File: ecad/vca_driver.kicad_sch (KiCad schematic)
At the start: 5 parts, among them Q2 Q_PNP, Q3 Q_NPN, U1 MCP6001R

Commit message: stuff
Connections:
- net DRV_CURR_Vref: no longer U1.3 (+)
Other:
- note added: "level-shifter stage"
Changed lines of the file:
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@@
+		)
+	)
+	(text "level-shifter stage"
+		(exclude_from_sim no)
+		(at 74.676 91.44 0)
+		(effects
+			(font
+				(size 1.27 1.27)
+			)
 		)
 	)
@@
 	(hierarchical_label "DRV_CURR_Vref"
 		(shape input)
-		(at 95.25 91.44 180)
+		(at 63.5 91.44 180)
 		(effects
 			(font
@@
 		)
 	)
-	(group ""
-		(members "7da5fe76-c194-4e79-b321-c29380be2a89" "7fe1ba20-d693-422a-b992-88df42c37689"
-			"9cf646c3-572a-464c-8c83-e4a098683738"
-		)
-	)

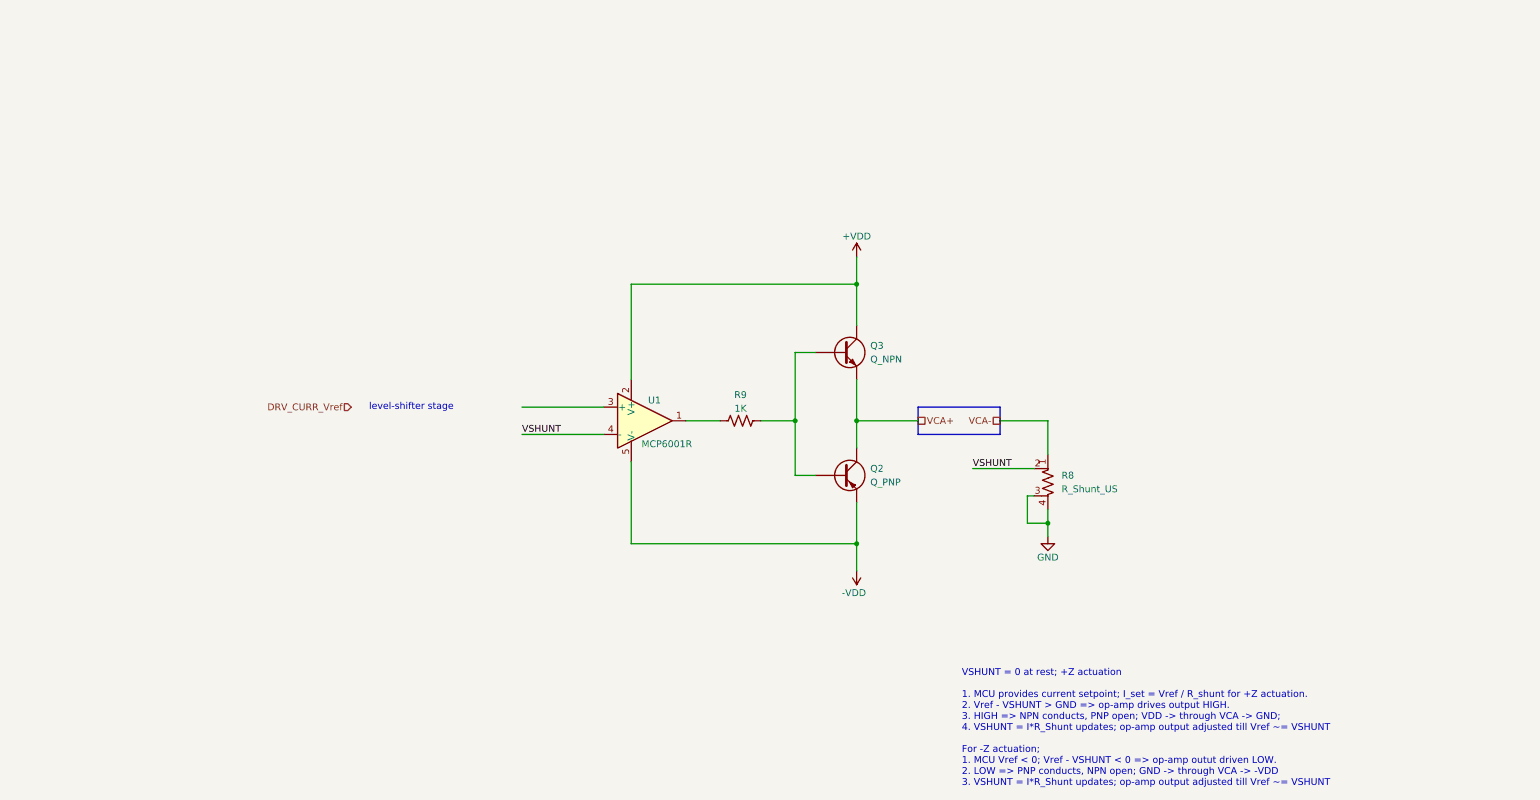
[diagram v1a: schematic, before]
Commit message: vca op-amp, transistor selection; heat calcs
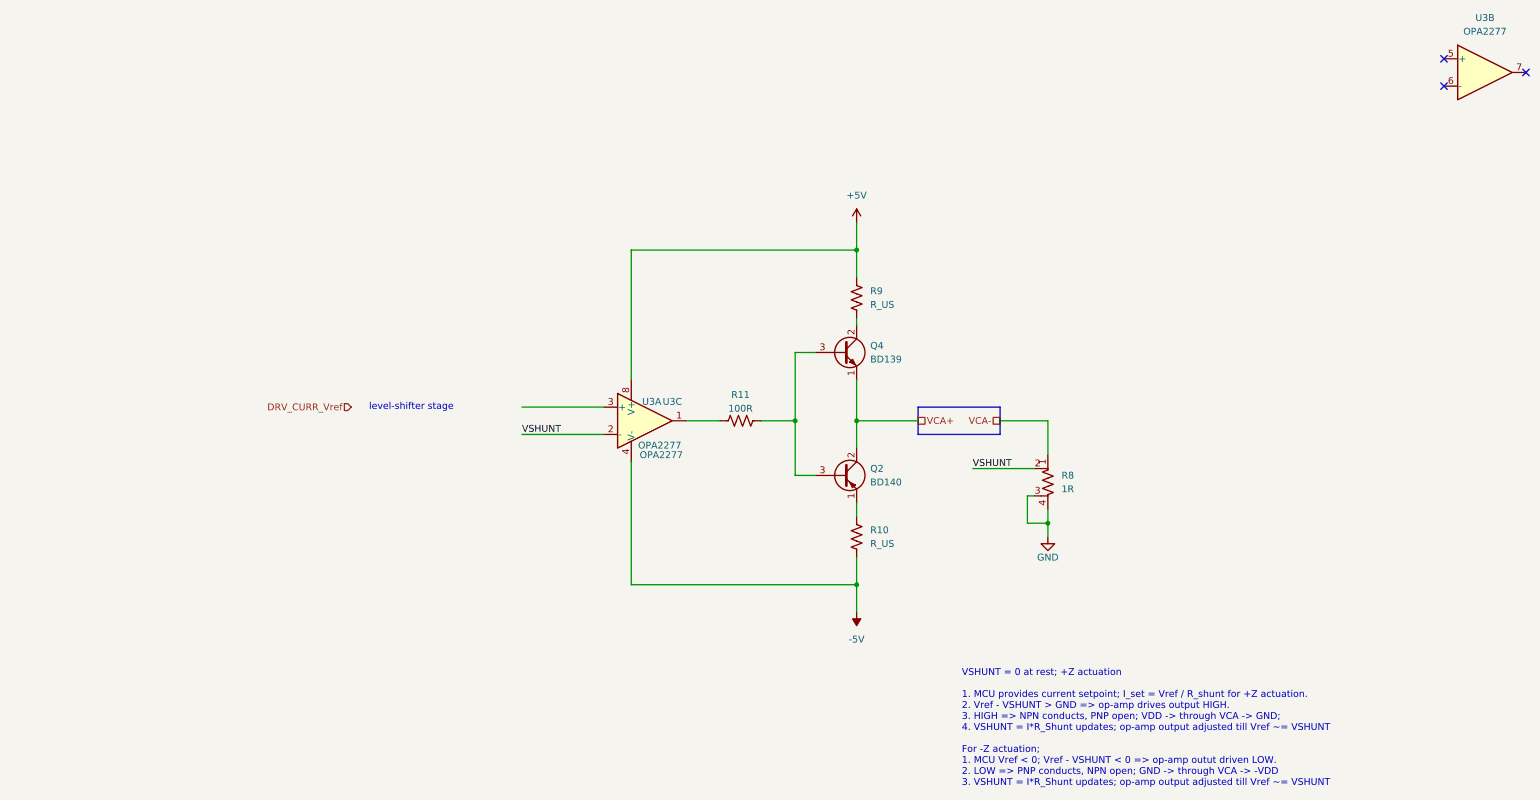
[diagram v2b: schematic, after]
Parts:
- removed Q2: Q_PNP, symbol Device:Q_PNP
- removed Q3: Q_NPN, symbol Device:Q_NPN
- removed U1: MCP6001R, Package_TO_SOT_SMD:SOT-23-5, symbol Amplifier_Operational:MCP6001R
- added Q2: BD140, Package_TO_SOT_THT:TO-126-3_Vertical, symbol Transistor_BJT:BD140
- added Q4: BD139, Package_TO_SOT_THT:TO-126-3_Vertical, symbol Transistor_BJT:BD139
- added R10: R_US, symbol Device:R_US
- added R11: 100R, symbol Device:R_US
- added U3: OPA2277, symbol Amplifier_Operational:OPA2277
- R8: value R_Shunt_US -> 1R
- R9: value 1K -> R_US
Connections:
- net VCA+: now also Q2.2 (C), Q4.1 (E)
- net VSHUNT: now also U3.2 (-)
- net at R9.2: now also Q4.2 (C)
- net +5V: now reaches R9.1
- net +5V: now also U3.8 (V+)
- new net: R11.2, U3.1
- new net: Q2.1 (E), R10.1
- new net: Q2.3 (B), Q4.3 (B), R11.1
- new net -5V: R10.2, U3.4 (V-)
- no-connect marks 0 -> 3

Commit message: more sizing
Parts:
- added C5, C9: 10uF, symbol Device:C_Small
- added R12: 100R, symbol Device:R_US
- R10, R9: value R_US -> 2-10R
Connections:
- net +5V: now also C5.1
- net -5V: now also C9.1
- net GND: now also C5.2, C9.2
- net at R11.2, U3.1: now also R12.2
- net at Q4.3 (B), R11.1: no longer Q2.3 (B)
- new net: Q2.3 (B), R12.1
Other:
- moved on the sheet: Q4, R11, R9

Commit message: pp
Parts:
- added C10, C11: 0.1uF, symbol Device:C_Small
- added C12: 10nF, symbol Device:C_Small
- added D2: BAT54W, Package_TO_SOT_SMD:SOT-323_SC-70, symbol Diode:BAT54W
- added R13: 1K, symbol Device:R_US
- added R14: 47K, symbol Device:R_US
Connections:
- net +5V: now also C10.1
- net -5V: now also C11.1
- net GND: now also C10.2, C11.2, R14.2
- net VCA+: now also Q2.1 (E); no longer Q2.2 (C)
- net VSHUNT: now also R13.1; no longer U3.2 (-)
- net at R11.2, R12.2, U3.1: now also C12.2
- net at U3.3 (+): now also R14.1
- net at R10.1: now also Q2.2 (C); no longer Q2.1 (E)
- new net: C12.1, R13.2, U3.2 (-)
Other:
- moved on the sheet: C5, C9, U3A, U3C

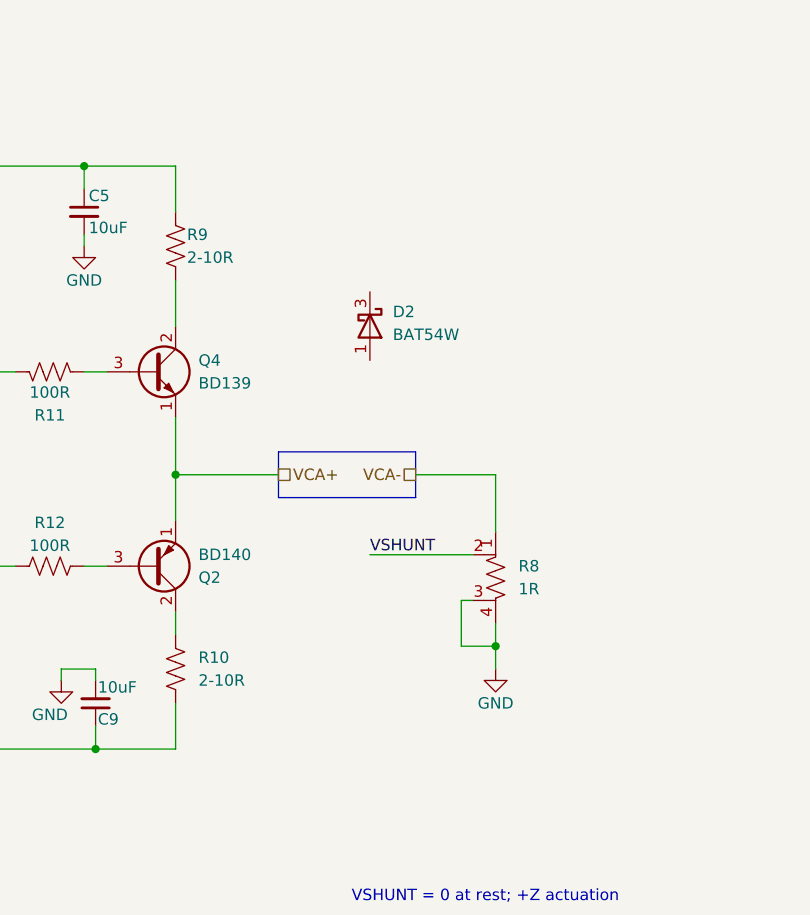
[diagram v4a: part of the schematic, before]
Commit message: diodes for L di/dt
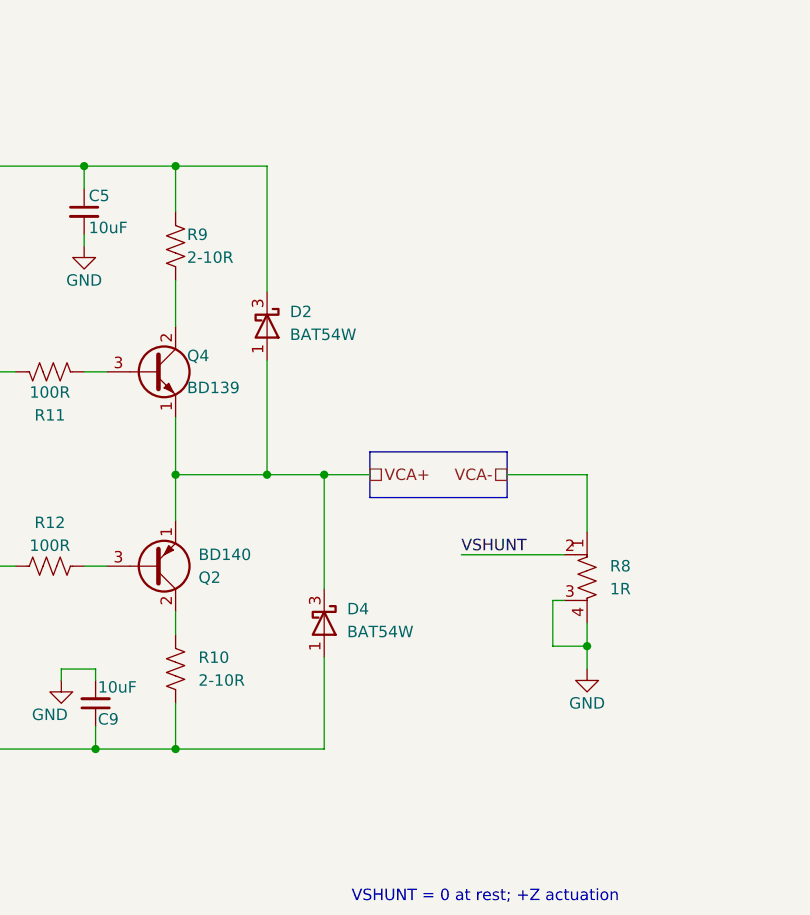
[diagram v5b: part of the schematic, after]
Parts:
- added D4: BAT54W, Package_TO_SOT_SMD:SOT-323_SC-70, symbol Diode:BAT54W
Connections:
- net +5V: now also D2.3 (K)
- net -5V: now also D4.1 (A)
- net VCA+: now also D2.1 (A), D4.3 (K)
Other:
- moved on the sheet: D2, R8

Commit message: vca sims
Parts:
- added R19: 500K, symbol Device:R_US
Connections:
- net at C12.1, R13.2, U3.2 (-): now also R19.1
- net at C12.2, R11.2, R12.2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: now also R19.2
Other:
- note added: "Some sort of clamp to limit max Vref to ~0.3V"
- moved on the sheet: C12
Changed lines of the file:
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@@
+		)
+	)
+	(text "Some sort of clamp to limit max Vref to ~0.3V"
+		(exclude_from_sim no)
+		(at 77.978 82.042 0)
+		(effects
+			(font
+				(size 1.27 1.27)
+			)
 		)
 	)
@@
 	)
 	(junction
+		(at 100.33 104.14)
+		(diameter 0)
+		(color 0 0 0 0)
+	)
+	(junction
 		(at 100.33 96.52)
 		(diameter 0)
@@
 	(junction
 		(at 148.59 124.46)
+		(diameter 0)
+		(color 0 0 0 0)
+	)
+	(junction
+		(at 123.19 104.14)
 		(diameter 0)
 		(color 0 0 0 0)
@@
 	(wire
 		(pts
+			(xy 100.33 104.14) (xy 100.33 96.52)
+		)
+		(stroke
+			(width 0)
+			(type default)
+		)
+	)
+	(wire
+		(pts
 			(xy 97.79 96.52) (xy 100.33 96.52)
 		)
@@
 	(wire
 		(pts
+			(xy 111.76 109.22) (xy 100.33 109.22)
+		)
+		(stroke
+			(width 0)
+			(type default)
+		)
+	)
+	(wire
+		(pts
 			(xy 157.48 119.38) (xy 157.48 124.46)
 		)
@@
 	(wire
 		(pts
-			(xy 118.11 105.41) (xy 123.19 105.41)
+			(xy 118.11 104.14) (xy 123.19 104.14)
 		)
 		(stroke
@@
 	(wire
 		(pts
+			(xy 123.19 104.14) (xy 123.19 109.22)
+		)
+		(stroke
+			(width 0)
+			(type default)
+		)
+	)
+	(wire
+		(pts
 			(xy 135.89 82.55) (xy 139.7 82.55)
 		)
@@
 	(wire
 		(pts
+			(xy 119.38 109.22) (xy 123.19 109.22)
+		)
+		(stroke
+			(width 0)
+			(type default)
+		)
+	)
+	(wire
+		(pts
 			(xy 157.48 72.39) (xy 157.48 77.47)
 		)
@@
 	(wire
 		(pts
-			(xy 113.03 105.41) (xy 100.33 105.41)
+			(xy 113.03 104.14) (xy 100.33 104.14)
 		)
 		(stroke
@@
 	(wire
 		(pts
+			(xy 123.19 104.14) (xy 123.19 93.98)
+		)
+		(stroke
+			(width 0)
+			(type default)
+		)
+	)
+	(wire
+		(pts
 			(xy 147.32 67.31) (xy 147.32 68.58)
 		)
@@
 	(wire
 		(pts
-			(xy 100.33 105.41) (xy 100.33 96.52)
-		)
-		(stroke
-			(width 0)
-			(type default)
-		)
-	)
-	(wire
-		(pts
 			(xy 203.2 113.03) (xy 203.2 115.57)
 		)
@@
 	(wire
 		(pts
+			(xy 100.33 104.14) (xy 100.33 109.22)
+		)
+		(stroke
+			(width 0)
+			(type default)
+		)
+	)
+	(wire
+		(pts
 			(xy 71.12 91.44) (xy 104.14 91.44)
 		)
@@
 		(pts
 			(xy 135.89 93.98) (xy 135.89 82.55)
-		)
-		(stroke
-			(width 0)
-			(type default)
-		)
-	)
-	(wire
-		(pts
-			(xy 123.19 105.41) (xy 123.19 93.98)
 		)
 		(stroke
@@
 	(symbol
 		(lib_id "Device:C_Small")
-		(at 115.57 105.41 90)
+		(at 115.57 104.14 90)
 		(unit 1)
 		(body_style 1)
@@
 		(dnp no)
 		(property "Reference" "C12"
-			(at 114.808 104.14 90)
+			(at 114.808 102.87 90)
 			(show_name no)
 			(do_not_autoplace no)
@@
 		)
 		(property "Value" "10nF"
-			(at 121.412 104.14 90)
+			(at 121.412 102.87 90)
 			(show_name no)
 			(do_not_autoplace no)
@@
 		)
 		(property "Footprint" ""
-			(at 115.57 105.41 0)
+			(at 115.57 104.14 0)
 			(hide yes)
 			(show_name no)
@@
 		)
 		(property "Datasheet" ""
-			(at 115.57 105.41 0)
+			(at 115.57 104.14 0)
 			(hide yes)
 			(show_name no)
@@
 		)
 		(property "Description" "Unpolarized capacitor, small symbol"
-			(at 115.57 105.41 0)
+			(at 115.57 104.14 0)
 			(hide yes)
 			(show_name no)
@@
 					(unit 1)
 				)
+			)
+		)
+	)
+	(symbol
+		(lib_id "Device:R_US")
+		(at 115.57 109.22 90)
+		(mirror x)
+		(unit 1)
+		(body_style 1)
+		(exclude_from_sim no)
+		(in_bom yes)
+		(on_board yes)
+		(in_pos_files yes)
+		(dnp no)
+		(property "Reference" "R19"
+			(at 112.522 107.95 90)
+			(show_name no)
+			(do_not_autoplace no)
+			(effects
+				(font
+					(size 1.27 1.27)
+				)
+			)
+		)
+		(property "Value" "500K"
+			(at 119.38 107.95 90)
+			(show_name no)
+			(do_not_autoplace no)
+			(effects
+				(font
+					(size 1.27 1.27)
+				)
+			)
+		)
+		(property "Footprint" ""
+			(at 115.824 110.236 90)
+			(hide yes)
+			(show_name no)
+			(do_not_autoplace no)
+			(effects
+				(font
+					(size 1.27 1.27)
+				)
+			)
+		)
+		(property "Datasheet" ""
+			(at 115.57 109.22 0)
+			(hide yes)
+			(show_name no)
+			(do_not_autoplace no)
+			(effects
+				(font
+					(size 1.27 1.27)
+				)
+			)
+		)
+		(property "Description" "Resistor, US symbol"
+			(at 115.57 109.22 0)
+			(hide yes)
+			(show_name no)
+			(do_not_autoplace no)
+			(effects
+				(font
+					(size 1.27 1.27)
+				)
+			)
+		)
+		(pin "2"
+		)
+		(pin "1"
+		)
+		(instances
+			(project "afm"
+				(path "/62de9aa8-4539-4ecb-8acc-2c7a46b3005b/152e488a-5c59-4955-a770-fd5dc463781b"
+					(reference "R19")
+					(unit 1)
+				)

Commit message: close
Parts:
- C12: value 10nF -> 4.7nF
- R19: value 500K -> 3M
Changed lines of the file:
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@@
 			)
 		)
-		(property "Value" "10nF"
+		(property "Value" "4.7nF"
 			(at 121.412 102.87 90)
 			(show_name no)
@@
 			)
 		)
-		(property "Value" "500K"
+		(property "Value" "3M"
 			(at 119.38 107.95 90)
 			(show_name no)

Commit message: vca drivec almost done
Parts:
- added Q5: BD139, Package_TO_SOT_THT:TO-126-3_Vertical, symbol Transistor_BJT:BD139
- added R20: 2R, symbol Device:R_US
- added R21: 2.2K, symbol Device:R_US
- C12: value 4.7nF -> 1.5nF
- R10, R9: value 2-10R -> 2R
- R12: value 100R -> 2R
- R14: value 47K -> 10K
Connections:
- net +5V: now also Q4.2 (C), R21.1; no longer R9.1
- net -5V: now also C9.2, Q2.2 (C); no longer C9.1, R10.2
- net GND: now also C9.1; no longer C9.2
- net VCA+: now also R10.1, R9.2; no longer Q2.1 (E), Q4.1 (E)
- net at C12.2, R11.2, R19.2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: no longer R12.2
- net at R12.1: now also Q4.3 (B), Q5.2 (C), R21.2; no longer Q2.3 (B)
- net at R11.1: now also Q2.3 (B), Q5.1 (E), R20.2; no longer Q4.3 (B)
- new net: Q5.3 (B), R12.2, R20.1
- new net: Q4.1 (E), R9.1
- new net: Q2.1 (E), R10.2
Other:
- moved on the sheet: C10, C12, C5, C9, D2, D4, Q2, Q4, R10, R11, R13, R14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
